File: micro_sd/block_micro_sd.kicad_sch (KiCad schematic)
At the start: 10 parts

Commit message: [Rushil] small change
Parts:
- MICRO_SD1: symbol TF-01A:TF-01A -> Library:TF-01A
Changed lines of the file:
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@@
 	)
 	(symbol
-		(lib_id "TF-01A:TF-01A")
+		(lib_id "Library:TF-01A")
 		(at 127 114.3 0)
 		(unit 1)

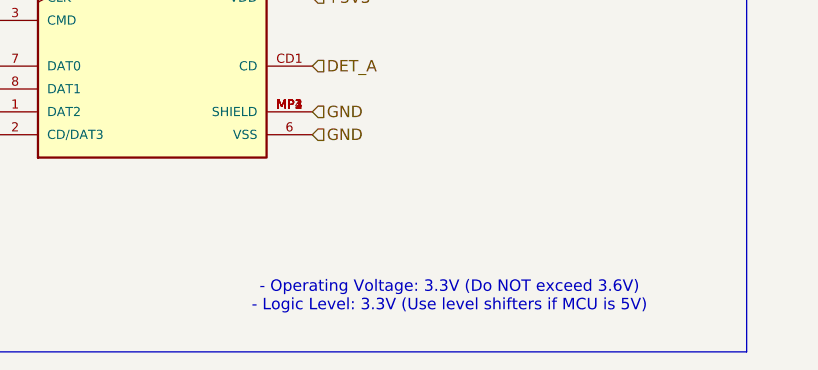
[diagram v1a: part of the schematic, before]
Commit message: [Rushil] added ams1117-3.3 block and did some clean up in schematic info part
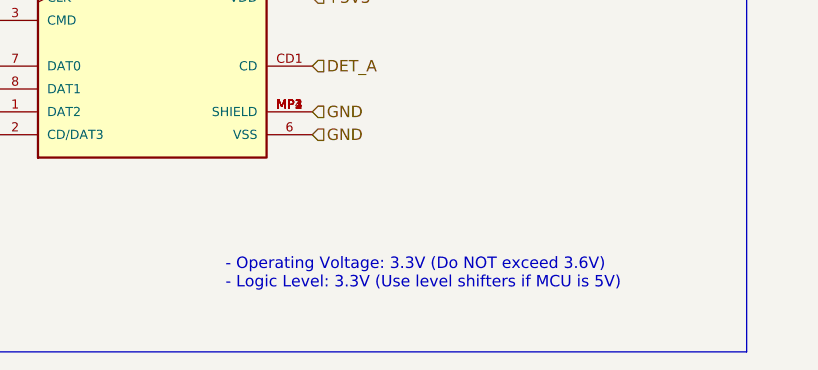
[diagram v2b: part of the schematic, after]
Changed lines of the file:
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@@
 	(text "- Operating Voltage: 3.3V (Do NOT exceed 3.6V)\n- Logic Level: 3.3V (Use level shifters if MCU is 5V)"
 		(exclude_from_sim no)
-		(at 160.02 139.954 0)
+		(at 135.128 137.414 0)
 		(effects
 			(font
 				(size 1.27 1.27)
 			)
+			(justify left)
 		)
 	)

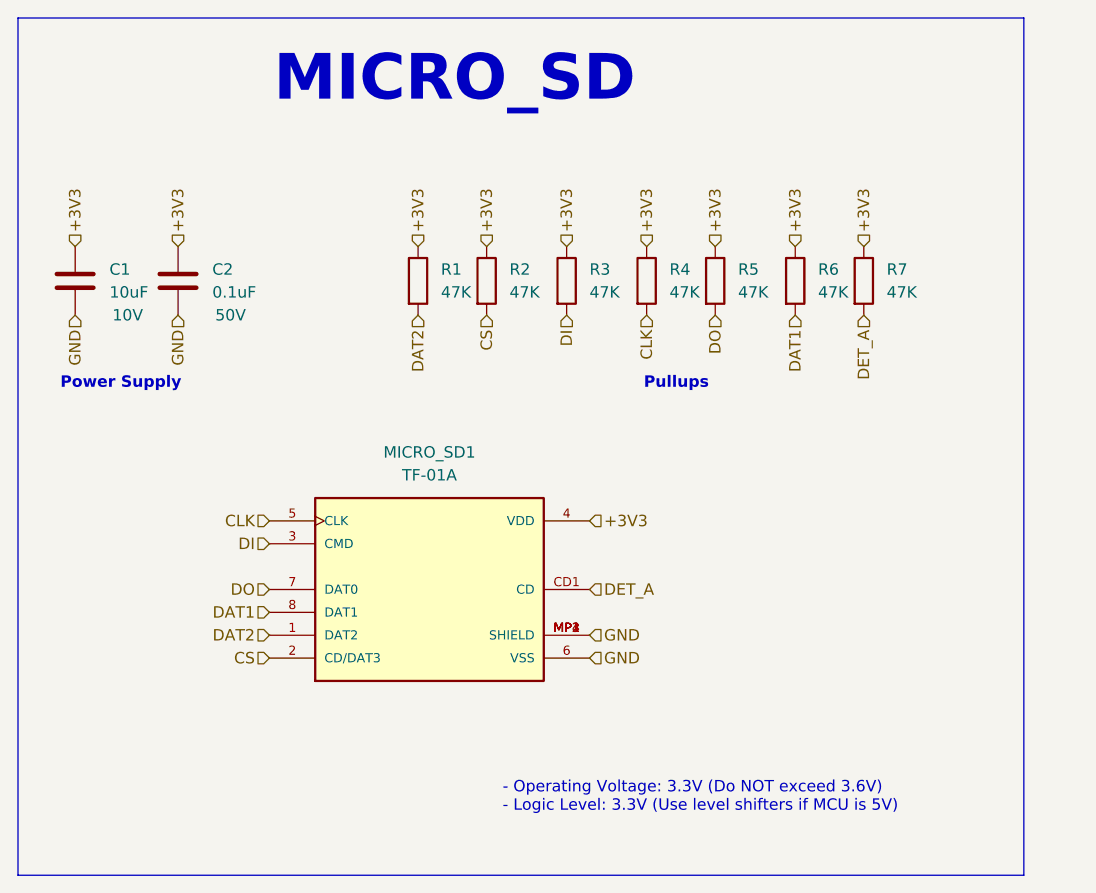
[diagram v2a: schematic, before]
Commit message: fixed microsd
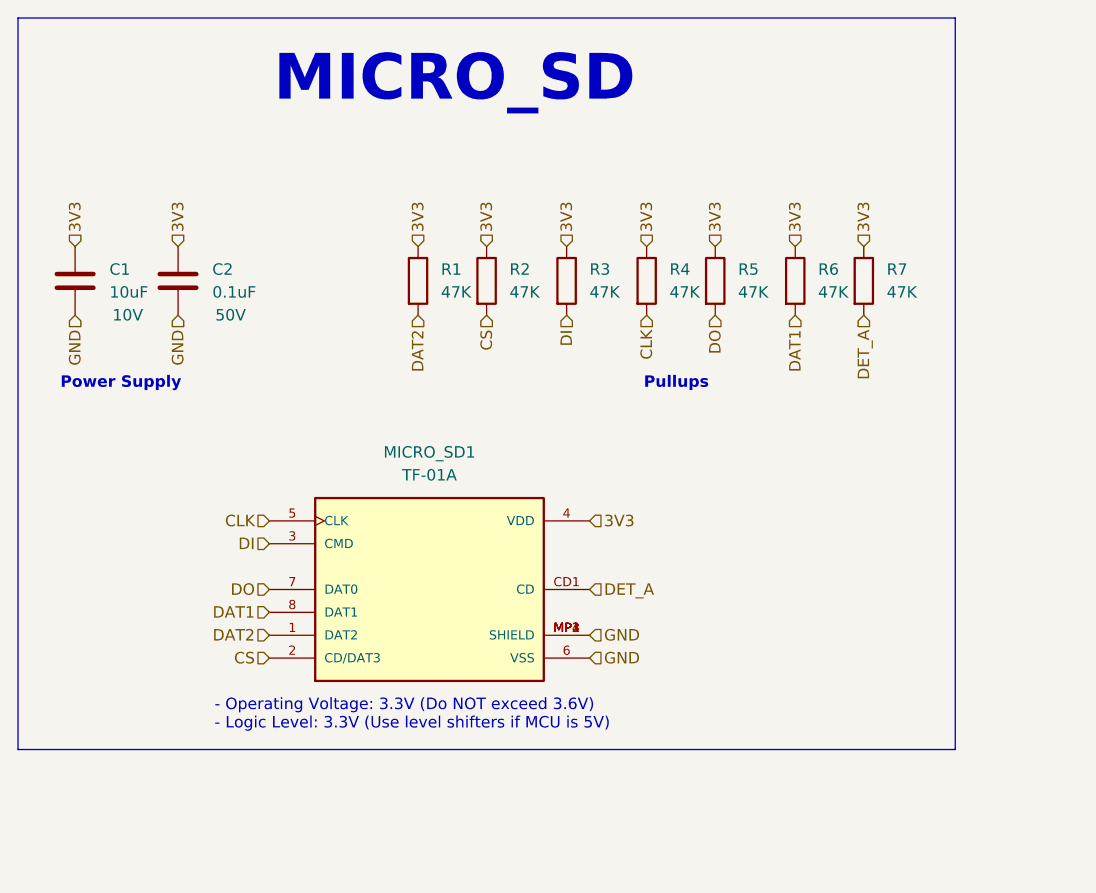
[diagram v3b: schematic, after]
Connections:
- net +3V3 renamed 3V3
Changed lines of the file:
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@@
 	(rectangle
 		(start 81.28 50.8)
-		(end 193.04 146.05)
+		(end 185.42 132.08)
 		(stroke
 			(width 0)
@@
 	(text "- Operating Voltage: 3.3V (Do NOT exceed 3.6V)\n- Logic Level: 3.3V (Use level shifters if MCU is 5V)"
 		(exclude_from_sim no)
-		(at 135.128 137.414 0)
+		(at 103.124 128.27 0)
 		(effects
 			(font
@@
 		)
 	)
-	(hierarchical_label "+3V3"
+	(hierarchical_label "3V3"
 		(shape input)
 		(at 142.24 76.2 90)
@@
 		)
 	)
-	(hierarchical_label "+3V3"
+	(hierarchical_label "3V3"
 		(shape input)
 		(at 133.35 76.2 90)
@@
 		)
 	)
-	(hierarchical_label "+3V3"
+	(hierarchical_label "3V3"
 		(shape input)
 		(at 144.78 106.68 0)
@@
 		)
 	)
-	(hierarchical_label "+3V3"
+	(hierarchical_label "3V3"
 		(shape input)
 		(at 158.75 76.2 90)
@@
 		)
 	)
-	(hierarchical_label "+3V3"
+	(hierarchical_label "3V3"
 		(shape input)
 		(at 167.64 76.2 90)
@@
 		)
 	)
-	(hierarchical_label "+3V3"
+	(hierarchical_label "3V3"
 		(shape input)
 		(at 87.63 76.2 90)
@@
 		)
 	)
-	(hierarchical_label "+3V3"
+	(hierarchical_label "3V3"
 		(shape input)
 		(at 125.73 76.2 90)
@@
 		)
 	)
-	(hierarchical_label "+3V3"
+	(hierarchical_label "3V3"
 		(shape input)
 		(at 151.13 76.2 90)
@@
 		)
 	)
-	(hierarchical_label "+3V3"
+	(hierarchical_label "3V3"
 		(shape input)
 		(at 175.26 76.2 90)
@@
 		)
 	)
-	(hierarchical_label "+3V3"
+	(hierarchical_label "3V3"
 		(shape input)
 		(at 99.06 76.2 90)
